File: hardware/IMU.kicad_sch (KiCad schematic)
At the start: 37 parts, among them J1 Conn_01x10, J3 USB_B_Micro, J4 Conn_01x10, J6 UART, J8 IMU_Headers, J9 SWD, SW1 SW_Push, U2 HT75xx-1-SOT89, U3 ISM330DLCTR, U4 STM32F401RCT6TR, Y2 WE-XTAL_CFPX-104

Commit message: added spi
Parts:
- removed J4: Conn_01x10, Connector_PinHeader_2.54mm:PinHeader_1x10_P2.54mm_Vertical, symbol Connector_Generic:Conn_01x10
- removed R4: 10k?, Resistor_SMD:R_0805_2012Metric, symbol Device:R
- added J2: Conn_01x06, Connector_PinHeader_2.54mm:PinHeader_1x06_P2.54mm_Vertical, symbol Connector_Generic:Conn_01x06
- added J4: SPI_Headers, Connector_PinHeader_2.54mm:PinHeader_1x04_P2.54mm_Vertical, symbol Connector_Generic:Conn_01x04
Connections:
- net +3V3: no longer C11.1, C12.1, C2.1, C3.1, C4.1, C5.1, C6.1, C7.1, D2.2 (A), J6.1 (Pin_1), J8.3 (Pin_3), J9.1 (Pin_1), R1.1, U3.12 (CS), U3.5 (VDDIO), U3.8 (VDD), U4.1 (VBAT), U4.19 (VDD), U4.32 (VDD__1), U4.48 (VDD__2), U4.64 (VDD__3)
- net GND: now also J2.1 (Pin_1)
- net at U4.36 (PB15): now also J2.5 (Pin_5)
- net at U4.33 (PB12): now also J2.2 (Pin_2)
- net at U4.34 (PB13): now also J2.3 (Pin_3)
- net at U4.35 (PB14): now also J2.4 (Pin_4)
- net PA4 renamed SPI1_CS
- net SPI1_CS: now also J4.4 (Pin_4)
- net PA5 renamed SPI_SCK
- net SPI_SCK: now also J4.3 (Pin_3)
- net PA6 renamed SPI1_MISO
- net SPI1_MISO: now also J4.2 (Pin_2)
- net PA7 renamed SPI1_MOSI
- net SPI1_MOSI: now also J4.1 (Pin_1)
- new net PWR: C11.1, C12.1, C2.1, C3.1, C4.1, C5.1, C6.1, C7.1, D2.2 (A), J2.6 (Pin_6), J6.1 (Pin_1), J8.3 (Pin_3), J9.1 (Pin_1), R1.1, U3.12 (CS), U3.5 (VDDIO), U3.8 (VDD), U4.1 (VBAT), U4.19 (VDD), U4.32 (VDD__1), U4.48 (VDD__2), U4.64 (VDD__3)
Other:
- note added: "Test Headers for SPI"
- moved on the sheet: J8, J9

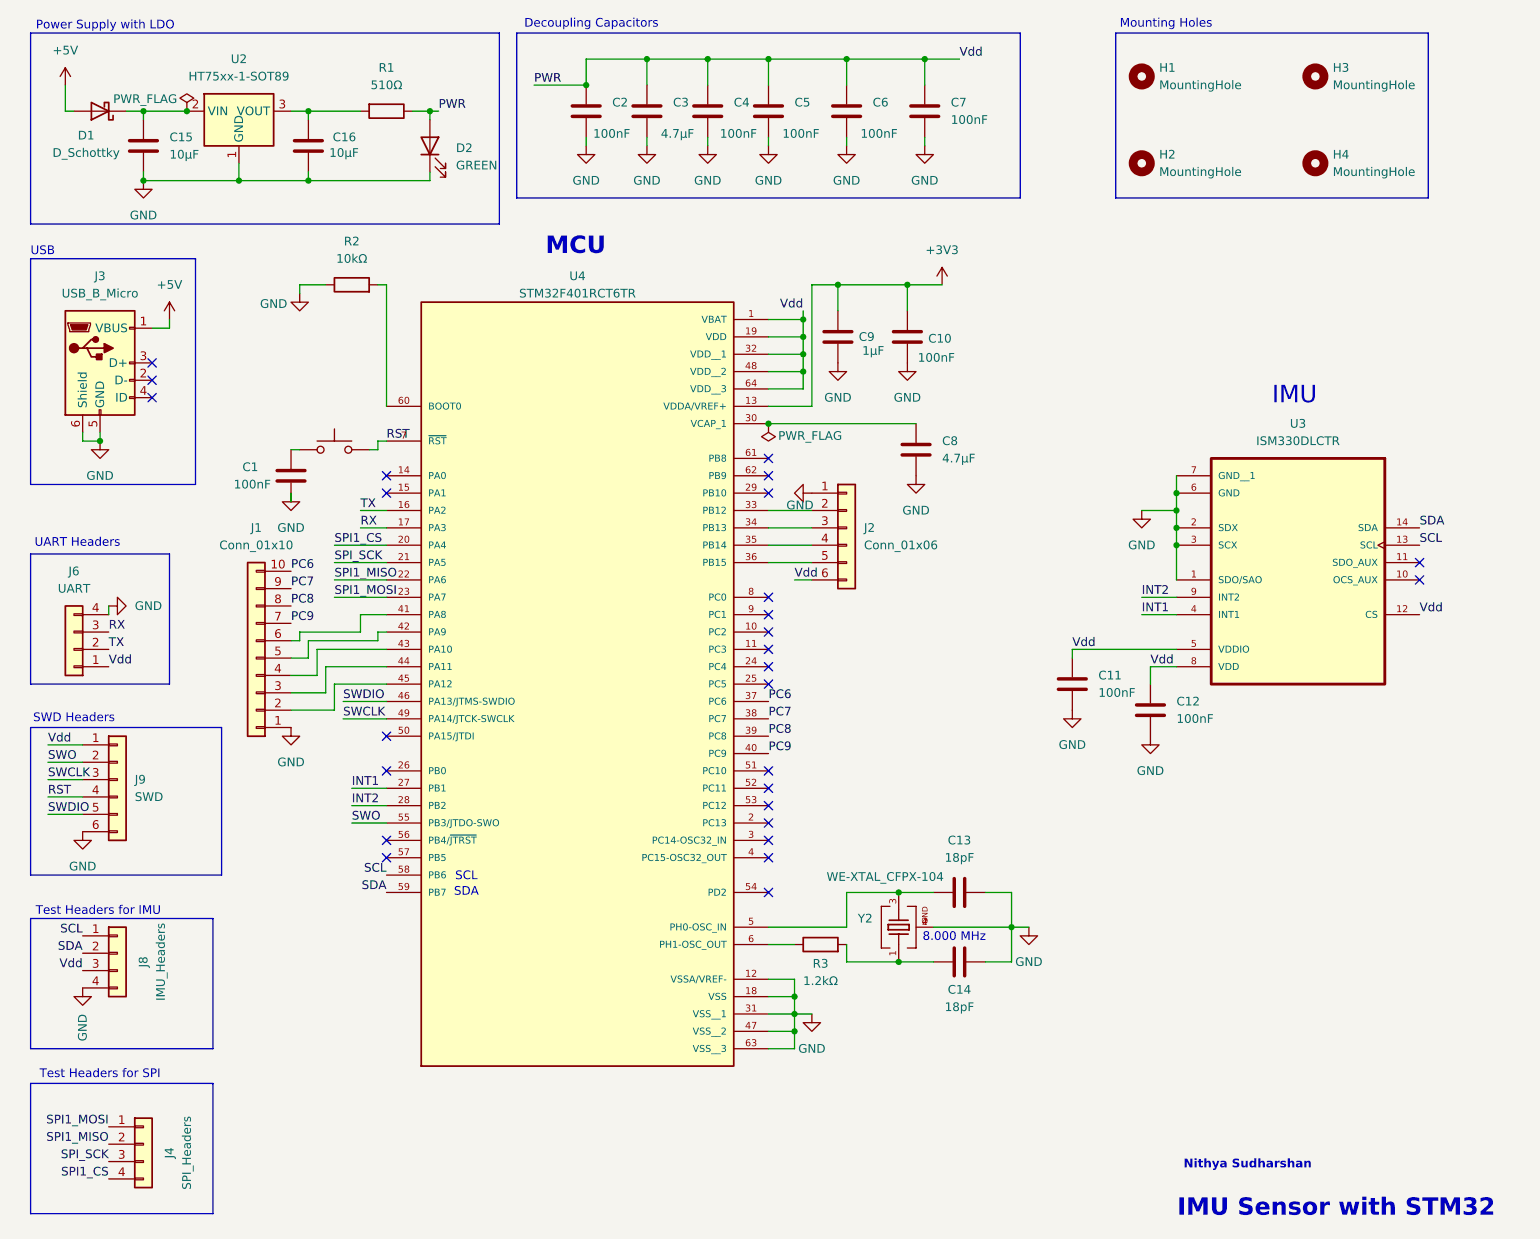
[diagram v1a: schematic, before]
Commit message: Fixed IMU
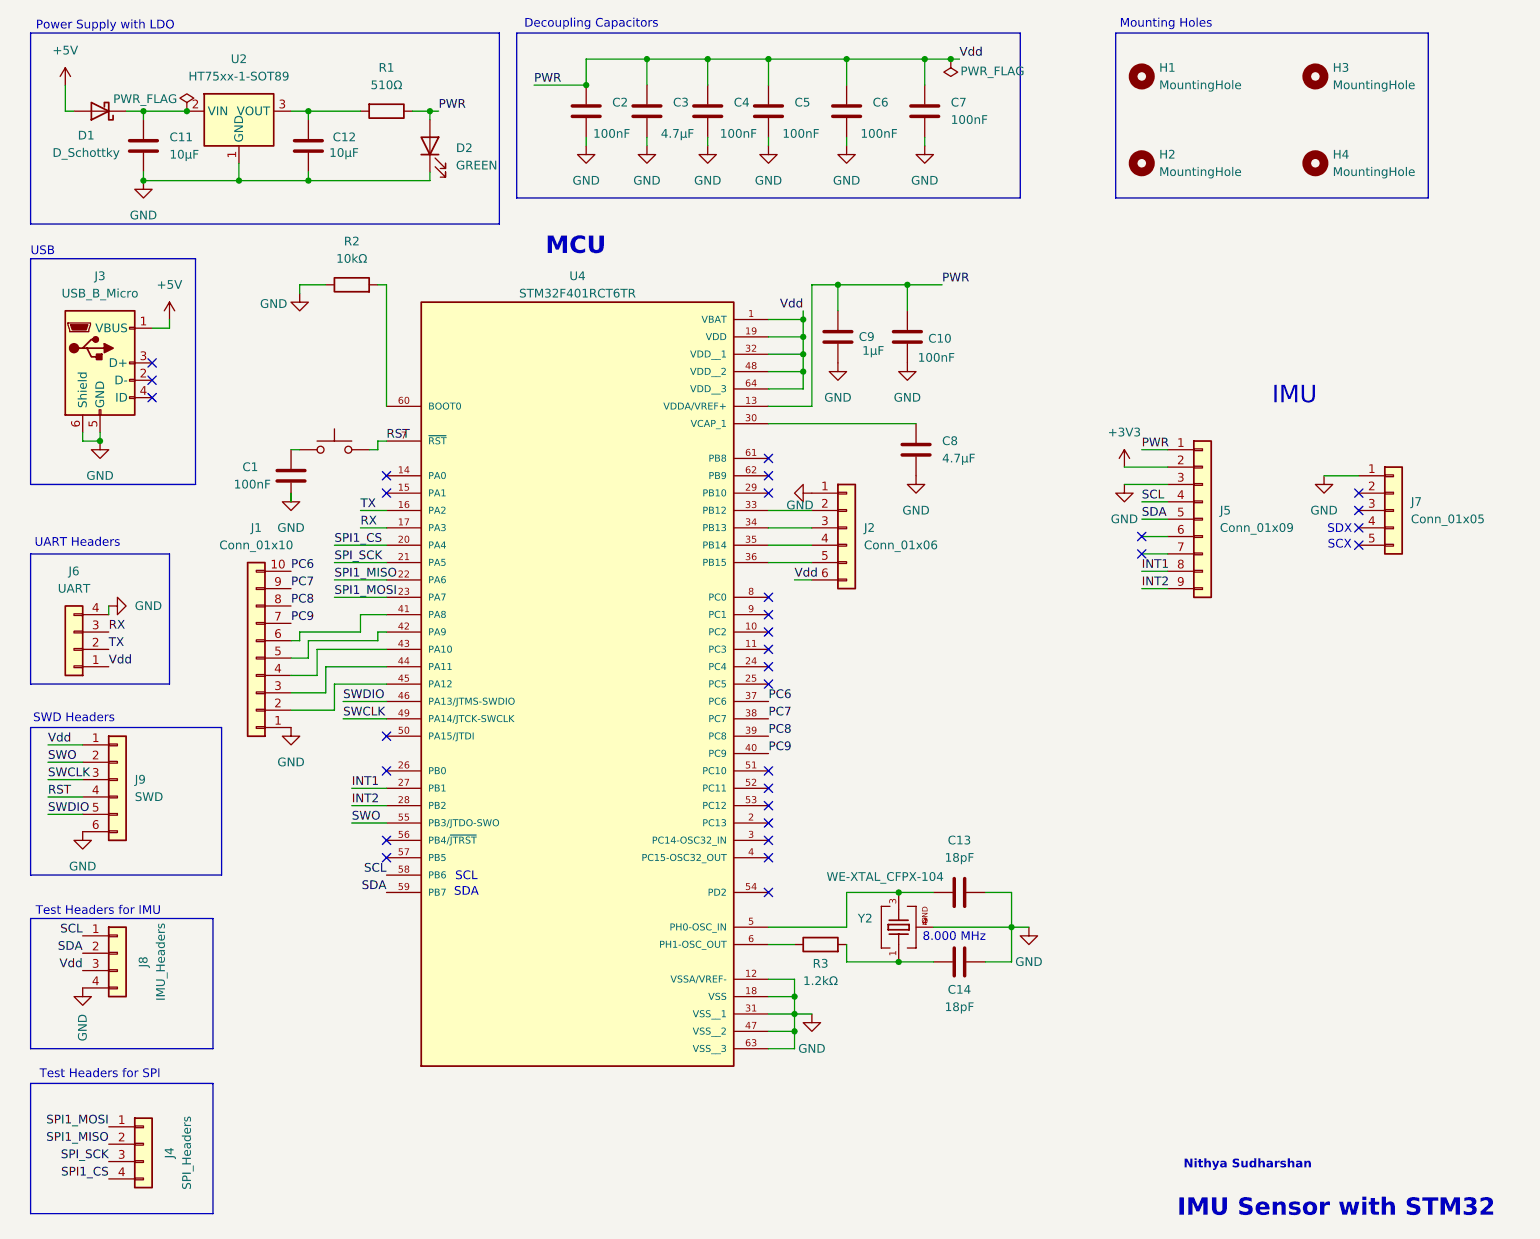
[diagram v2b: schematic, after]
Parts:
- removed C11, C12: 100nF, Capacitor_SMD:C_0805_2012Metric, symbol Device:C
- removed U3: ISM330DLCTR, My_library:PQFN50P250X300X86-14N, symbol My_library:ISM330DLCTR
- added J5: Conn_01x09, Connector_PinHeader_2.54mm:PinHeader_1x09_P2.54mm_Vertical, symbol Connector_Generic:Conn_01x09
- added J7: Conn_01x05, Connector_PinHeader_2.54mm:PinHeader_1x05_P2.54mm_Vertical, symbol Connector_Generic:Conn_01x05
- renumbered C15 to C11, C16 to C12
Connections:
- net +3V3: now also J5.2 (Pin_2); no longer C10.1, C9.1, U4.13 (VDDA/VREF+)
- net GND: now also J5.3 (Pin_3), J7.1 (Pin_1)
- net INT1: now also J5.8 (Pin_8)
- net INT2: now also J5.9 (Pin_9)
- net PWR: now also C10.1, C9.1, U4.13 (VDDA/VREF+), J5.1 (Pin_1)
- net SCL: now also J5.4 (Pin_4)
- net SDA: now also J5.5 (Pin_5)
- no-connect marks 27 -> 31
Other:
- note added: "SCX"
- note added: "SDX"
